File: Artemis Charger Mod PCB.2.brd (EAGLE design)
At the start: 99.1 x 96.5 mm, 156 parts, among them J1 MOLEX_CLICKMATE-2-VERTICAL, J2 MOLEX_CLICKMATE-4-VERTICAL, J3 MOLEX_CLICKMATE-2-VERTICAL, J4 MOLEX_CLICKMATE-2-VERTICAL, J5 MOLEX_CLICKMATE-2-VERTICAL, J6 MOLEX_CLICKMATE-4-VERTICAL, Q10 BSS138, Q11 BSS138, Q8 BSS138, Q9 BSS138, U10 TPS562219, U11 ISO7340, U12 ISO7340, U13 TPS562219, U14 MCP2515-TSSOP, U15 MCP2562, U16 CD4050BD, U17 CD4050BD, U18 CD4043B, U19 SN74LVC08ASOIC, U20 SN74LVC32ASOIC, U22 LTC1155, U23 CSD17506Q5A, U24 LTC1155, U25 CD4050BD, U26 CSD17506Q5A, U27 LTC1155, U28 CSD17506Q5A, U29 LTC1155, U3 MAX5812, U30 CSD17506Q5A, U31 LTC1155, U32 CSD17506Q5A, U33 LTC1155, U34 CSD17506Q5A, U49 TL7712A-SOIC, U8 MAX5812, U9 TPS562219

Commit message: DONE
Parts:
- moved R6 1.27 mm to (21.0, 58.4)
- moved C40 0.64 mm to (39.4, 50.2)
- moved U3 0.64 mm to (17.8, 58.4)
- moved U8 0.63 mm to (11.4, 58.4)
- moved Q8 0.63 mm to (41.3, 61.0)
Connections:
- removed net +5V/1_CURRENT_SENSE: O1.1
- net +3V3: now also O1.1
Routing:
- net GND1: track 386.0 -> 213.1 mm
- net GND: track 88.9 -> 61.7 mm
- net +3V3: track 117.8 -> 125.0 mm, vias 16 -> 17
- net +5V/1_CURRENT_SENSE: track 2.18 -> 0.00 mm, vias 1 -> 0
- net N$9: track 344.1 -> 342.3 mm
- net DRIVE_DISBALE_SIGNAL_3V3: track 101.3 -> 102.9 mm
- net N$7: track 47.1 -> 48.5 mm
- net N$1000: track 26.9 -> 27.8 mm
- net VBST_5V/1: track 6.99 -> 6.32 mm
- net VDD: track 152.9 -> 153.5 mm
- net N$58: track 97.7 -> 98.3 mm
- net N$4: track 6.07 -> 6.70 mm
- net RTDS_SOURCE: track 74.8 -> 75.4 mm
- net N$26: track 8.87 -> 9.40 mm
- net RSC_SIGNAL_3V3: track 78.6 -> 78.1 mm
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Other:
- board text added: "Formula Electric"
- board text added: "Missouri S&T"

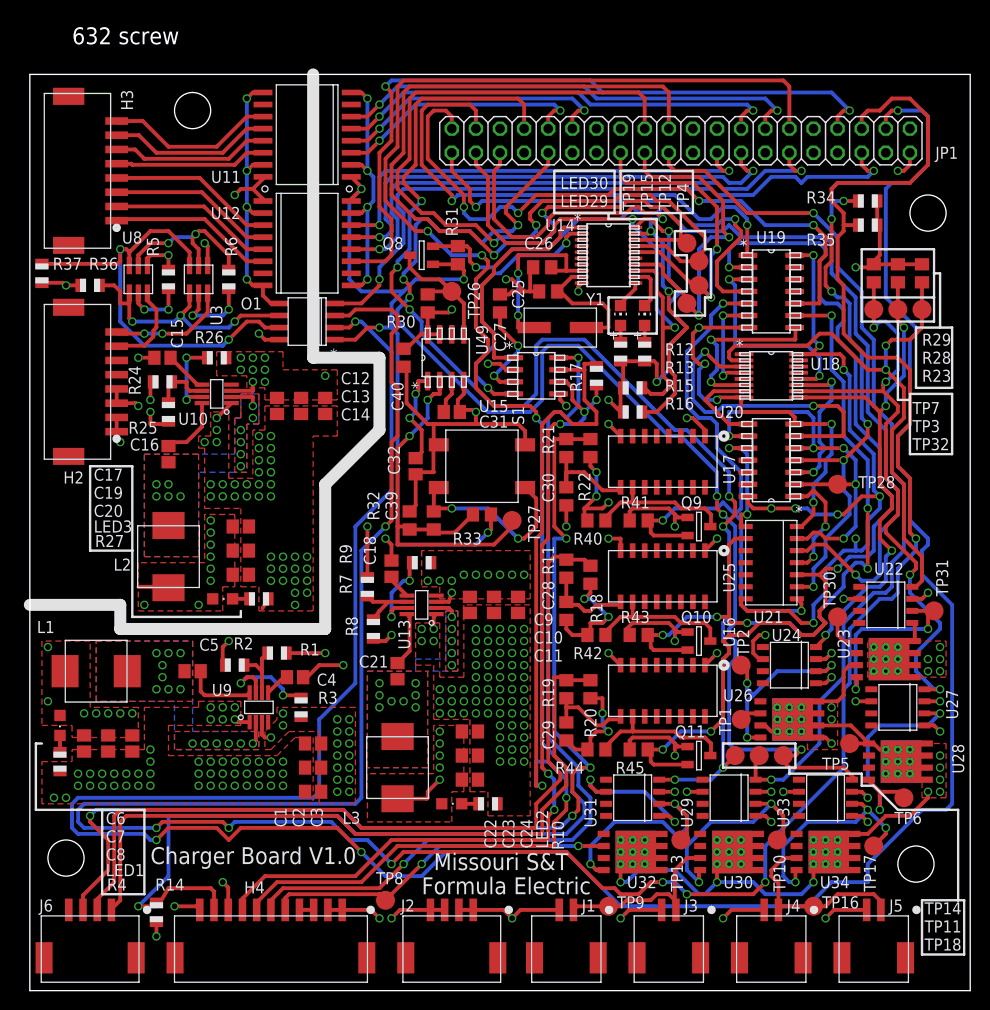
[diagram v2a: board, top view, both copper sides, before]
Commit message: Fixed list of errors: Too many vias around regulators
Make +5V plane in cover all area in isolated region

Make isolation barrier a simple rectangle

rotate +5v regulator (isolated area) 180deg so that the current path is more direct

More vias/planes at connectors

Give nets a descriptive name

Use vector font

U16/17/25 should combine into one part

bypass caps on ICs

U22/24/27/29/31/33 can be combined into 3 parts

RTDS_SOURCE is connected to FETs that it shouldn't be

U18 has a floating EN pin

use planes for current paths to the FETs, and make sure to connect to all of the pads (3 source, 4+pad drain)

Check pin current limits of connectors

Can use 10mil traces if needed for signals

Add mark to indicate pin 1 of RasPi connector

Watch mechanical clearances at the end of ICs, there are some that are really close

Q10/11 level shifters have pull downs. Does this work?

Label the connectors on the PCB so we know what they connect to.

Do we really need testpoints on every FET driver input/output?

Supply layer planes are a mess

Check RasPi power pins. There are multiple 5v and GND. Currently use 1 5V and no GND

RasPi Pin 6 is connected to the ground of one of the isolators, but not to the GND1 net

RasPi SPI interface is wired wrong

RasPi pin 39 is connected to the board as an I/O, but it is a GND pin
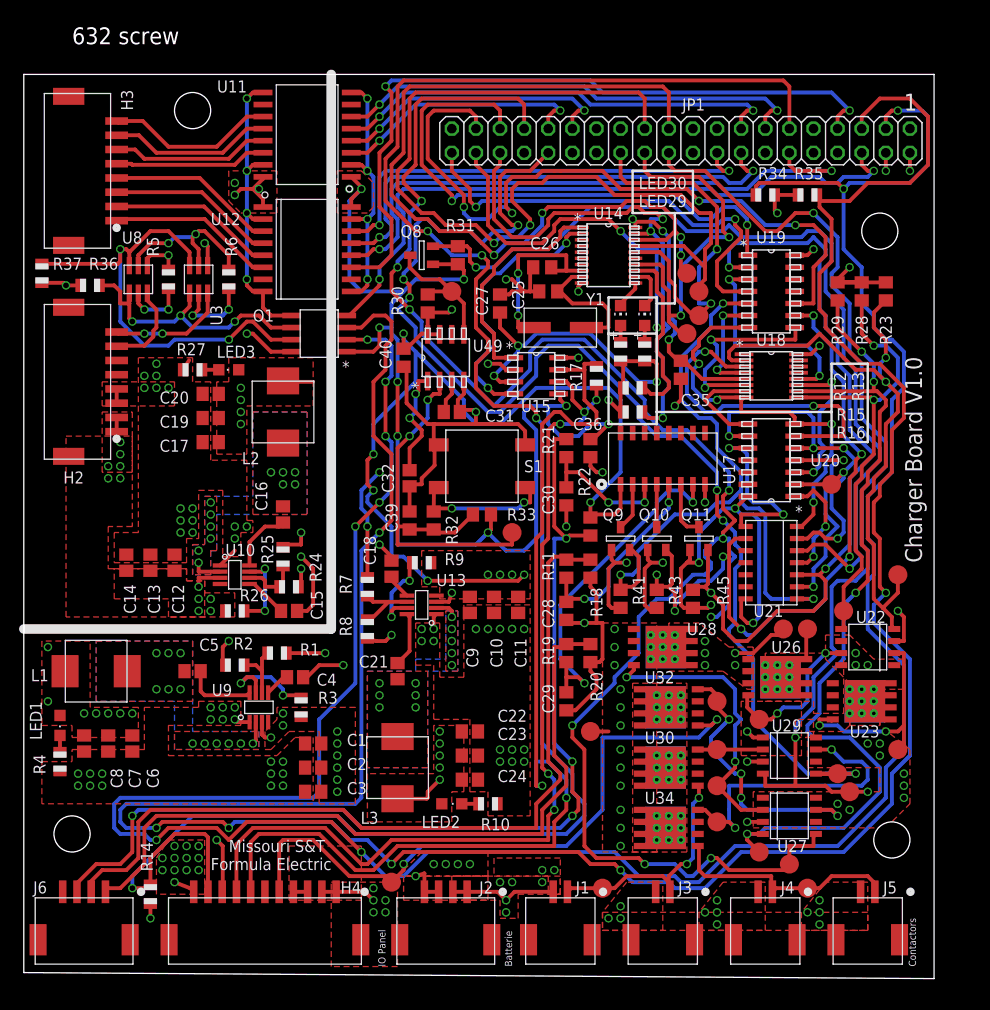
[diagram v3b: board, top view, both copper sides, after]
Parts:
- removed R40, R42, R44: 10k, rcl:R0805
- removed U16, U25: CD4050BD, FormE:SOIC-16
- removed U24, U31, U33: LTC1155, FormE:LT-SOL8
- added C35, C36: 1uF, rcl:C0805
- moved TP7 58.4 mm to (76.8, -1.91)
- moved TP3 32.3 mm to (85.7, 23.5)
- moved C15 29.8 mm to (27.3, 23.5), turned to 0 degrees
- moved TP32 28.1 mm to (91.4, 27.3)
- moved U28 27.5 mm to (66.7, 19.7)
- moved TP5 27.3 mm to (59.1, 10.8)
- moved R26 26.7 mm to (21.6, 23.5), turned to 0 degrees
- moved C14 26.7 mm to (10.2, 28.6), turned to 90 degrees
- moved R24 25.4 mm to (27.3, 26.0), turned to 0 degrees
- moved R27 25.1 mm to (17.1, 48.9), turned to 0 degrees
- moved LED3 24.1 mm to (21.0, 48.9), turned to 90 degrees
- moved C13 22.9 mm to (12.7, 28.6), turned to 90 degrees
- moved Q11 22.9 mm to (70.5, 31.1), turned to 0 degrees
- moved TP6 19.7 mm to (72.4, 5.08)
- moved C12 19.7 mm to (15.2, 28.6), turned to 90 degrees
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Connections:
- net MO renamed SO_SPI
- net N$10 renamed SCL1_I2C
- net N$1000 renamed SCL
- net N$11 renamed ADD
- net N$24 renamed ADJ_EMULATOR_IN_2
- net N$27 renamed ADJ_EMULATOR_IN_4
- net N$29 renamed ADJ_EMULATOR_IN_3
- net N$34 renamed LED_TO_PI_4
- net N$35 renamed LED_TO_PI_3
- net N$36 renamed LED_TO_PI_2
- net N$37 renamed LED_TO_PI_1
- net N$5 renamed ADJ_EMULATOR_IN_1
- net N$7 renamed SDA
- net N$70 renamed CS_SPI
- net RTDS_SOURCE2 renamed ACUMULATOR_CONTACTOR_SIGNAL
- net SCK renamed SCK_SPI
- removed net N$18: JP1.6, O1.4
- removed net N$48: H4.6, U15.8
- new net FET_CONNECT_1: TP30.TP, U23.1, U23.2, U23.3, U26.5, U26.6, U26.7, U26.8, U26.PAD, U26.PAD1, U26.VIA1, U26.VIA2, U26.VIA3, U26.VIA4, U26.VIA5, U26.VIA6, U26.VIA7, U26.VIA8, U26.VIA9
- new net FET_CONNECT_2: TP1.TP, U26.1, U26.2, U26.3, U28.5, U28.6, U28.7, U28.8, U28.PAD, U28.PAD1, U28.VIA1, U28.VIA2, U28.VIA3, U28.VIA4, U28.VIA5, U28.VIA6, U28.VIA7, U28.VIA8, U28.VIA9
- new net SDA1_I2C: JP1.3, O1.2, R34.2
- net +3V3: now also C35.1, C36.1, U14.20, U15.5, U18.16, U18.5, U19.14, U20.14, U21.14
- net +5V/1: now also JP1.4; no longer U14.20, U15.5
- net AMS_15V_FILTERED: now also U17.4; no longer R42.1, U25.10
- net AMS_BACK_TO_PI: now also JP1.37; no longer JP1.39
- net BSPD_FET_SIGNAL: now also U22.5; no longer U24.4
- net BSPD_FET_SIGNAL1: now also U27.5; no longer U31.4
- net BSPD_FET_SIGNAL3: now also U29.5; no longer U33.4
- net GND1: now also C35.2, C36.2, JP1.14, JP1.20, JP1.25, JP1.30, JP1.34, JP1.6, JP1.9, O1.4, U15.8; no longer R42.2, R44.2, U16.8, U24.3, U25.8, U31.3, U33.3
- net IMD_15V_FILTERED: now also U17.2; no longer R40.1, U17.10
- net INTERUPT_LINES_15V_FILTERED: now also U17.6; no longer R44.1, U16.10
- net INTERUPT_LINES_BACK_TO_PI: now also JP1.35; no longer JP1.37
- net N$43: now also U17.5; no longer U25.9
- net N$50: now also U17.7; no longer U16.9
- net N$53: now also U17.3; no longer U17.9
- net N$55: now also U22.7; no longer U24.2
- net N$59: now also U27.7; no longer U31.2
- net N$64: now also U29.7; no longer U33.2
- net N$9: no longer JP1.3, O1.2, R34.2
- net RTDS_SOURCE: no longer TP1.TP, TP30.TP, U23.1, U23.2, U23.3, U26.1, U26.2, U26.3, U26.5, U26.6, U26.7, U26.8, U26.PAD, U26.PAD1, U26.VIA1, U26.VIA2, U26.VIA3, U26.VIA4, U26.VIA5, U26.VIA6, U26.VIA7, U26.VIA8, U26.VIA9, U28.5, U28.6, U28.7, U28.8, U28.PAD, U28.PAD1, U28.VIA1, U28.VIA2, U28.VIA3, U28.VIA4, U28.VIA5, U28.VIA6, U28.VIA7, U28.VIA8, U28.VIA9
- net VDD: now also U22.8, U27.8, U29.8; no longer R40.2, U16.1, U18.16, U19.14, U20.14, U21.14, U24.1, U24.6, U25.1, U31.1, U31.6, U33.1, U33.6
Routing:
- net N$9: track 342.3 -> 23.0 mm, vias 10 -> 2
- net SDA1_I2C: track 0.00 -> 276.5 mm, vias 0 -> 9
- net +3V3: track 125.0 -> 227.2 mm, vias 17 -> 42
- net N$48: track 93.9 -> 0.00 mm, vias 2 -> 0
- net RTDS_SOURCE: track 75.4 -> 1.91 mm, vias 11 -> 12
- net N$18: track 71.4 -> 0.00 mm, vias 2 -> 0
- net GND1: track 213.1 -> 267.6 mm, vias 150 -> 80
- net BSPD_FET_SIGNAL1: track 131.8 -> 179.7 mm, vias 7 -> 9
- net VDD: track 153.5 -> 112.4 mm, vias 60 -> 37
- net ACUMULATOR_CONTACTOR_SIGNAL: track 38.0 -> 67.4 mm
- net RTDS_SIGNAL: track 64.4 -> 91.2 mm
- net N$50: track 9.63 -> 36.4 mm, vias 0 -> 2
- net DRIVE_DISBALE_SIGNAL_3V3: track 102.9 -> 83.4 mm, vias 4 -> 3
- net VCC: track 21.8 -> 5.96 mm, vias 10 -> 11
- net N$57: track 22.6 -> 6.86 mm, vias 2 -> 0
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- added copper zone on layer 1, net FET_CONNECT_1
- added copper zone on layer 1, net FET_CONNECT_2
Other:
- board size 99.1 x 96.5 mm -> 95.9 x 95.2 mm
- board text added: "1"
- board text added: "Batterie"
- board text added: "Contactors"
- board text added: "IO Panel"

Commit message: Started cleaning up layout
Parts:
- moved L2 3.81 mm to (26.7, 40.6)
- moved LED3 3.81 mm to (21.0, 45.1)
- moved R27 3.81 mm to (17.1, 45.1)
- moved C17 3.81 mm to (19.1, 37.5)
- moved C19 3.81 mm to (19.1, 40.0)
- moved C20 3.81 mm to (19.1, 42.5)
- moved C16 3.18 mm to (24.1, 31.8)
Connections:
- new net N$3: H4.3
- net GND1: now also JP1.39
- net N$25: now also H2.7; no longer H2.8
- net N$26: now also H2.8; no longer H2.7
- net N$42: no longer H4.3
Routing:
- net GND: track 67.7 -> 36.6 mm
- net GND1: track 267.6 -> 260.1 mm, vias 80 -> 79
- net +5V: track 36.1 -> 31.7 mm, vias 12 -> 13
- net VBST_5V: track 7.28 -> 3.03 mm
- net +5V/1: track 71.8 -> 68.0 mm, vias 18 -> 16
- net +3V3: track 227.2 -> 224.0 mm
- net VCC: track 5.96 -> 3.25 mm, vias 11 -> 0
- net SDA: track 50.3 -> 48.2 mm
- net N$42: track 1.50 -> 0.00 mm
- net SCL: track 29.6 -> 28.6 mm
- net N$26: track 9.40 -> 8.41 mm
- net LED_TO_PI_2: track 18.5 -> 17.5 mm
- net SW_5V: track 3.20 -> 2.26 mm, vias 11 -> 10
- net N$25: track 12.6 -> 13.1 mm, vias 2 -> 0
- net SW_3V3: track 2.39 -> 2.65 mm, vias 12 -> 10
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- removed copper zone on layer 15, net VCC
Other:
- board size 95.9 x 95.2 mm -> 95.9 x 94.6 mm
- board text removed: "632 screw"

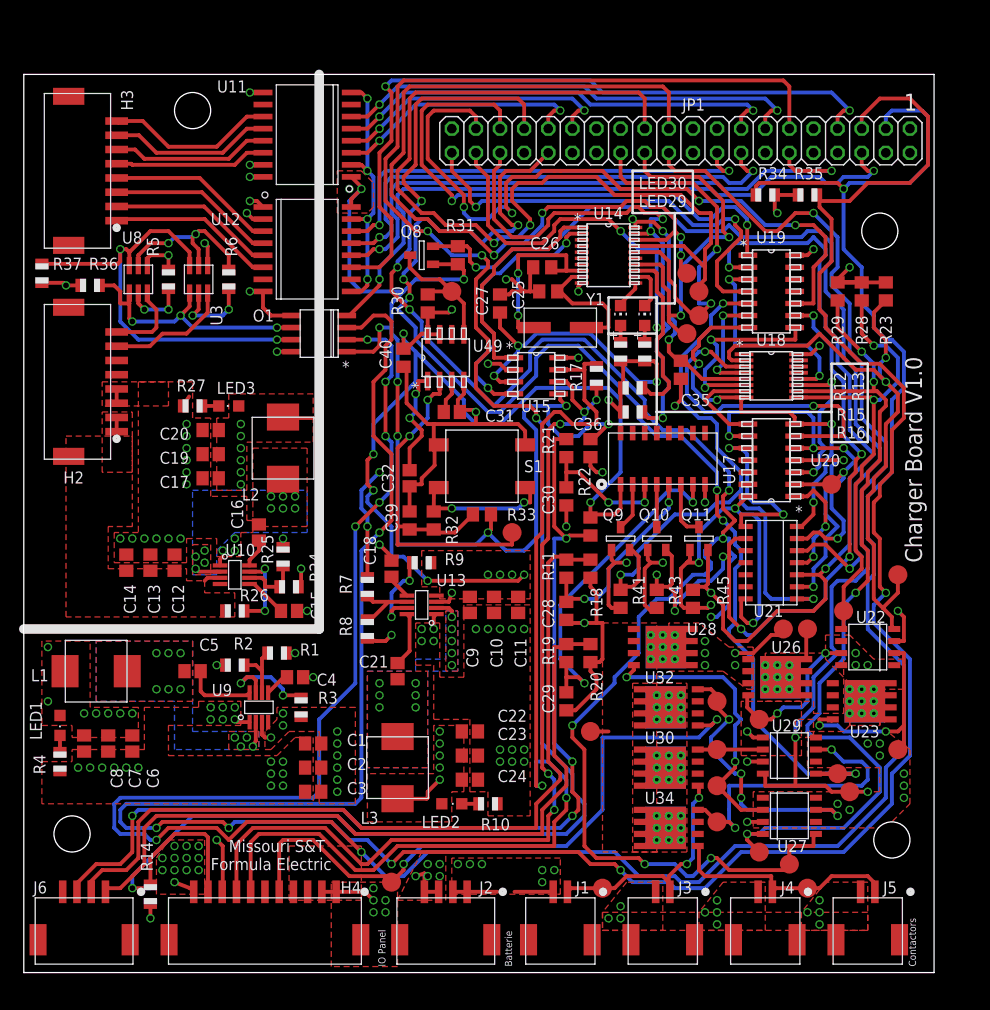
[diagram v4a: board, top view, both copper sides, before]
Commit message: Fixed second list of errors:  Decoupling capacitors
U11/12 EN pin is floating

Don't use solid planes at FET drivers

Lots of random vias

Planes from FETs to contactor connector

Connector labels

Cleanup supply layer planes

Isolation line needs to be thru center of isolators

unnecessary vias at raspi connector

SPI interface
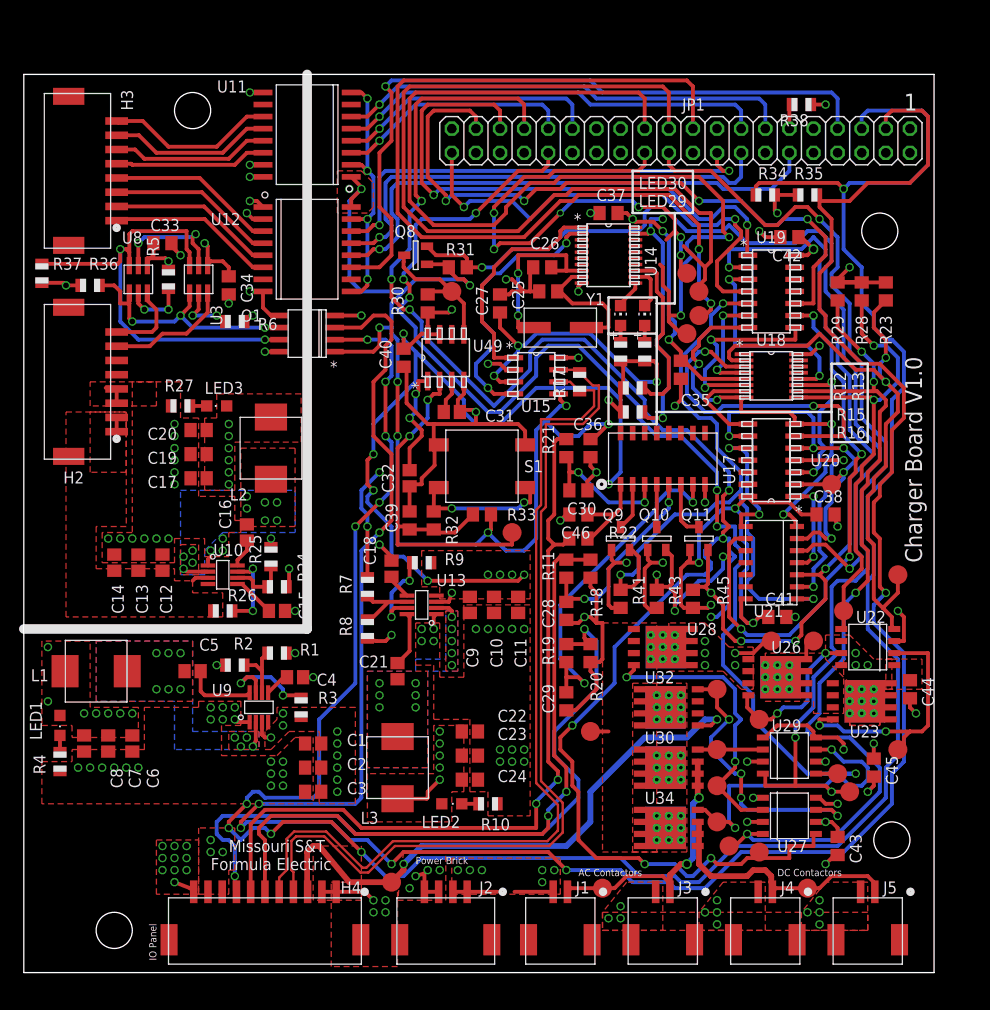
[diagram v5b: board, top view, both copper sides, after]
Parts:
- removed J6: MOLEX_CLICKMATE-4-VERTICAL, FormE:MOLEX-CLIKMATE-4-VERTICAL-HEADER
- removed R14: 10K, adafruit:R0805
- added C33, C34, C37, C38, C41, C42, C43, C44, C45, C46: 0.1uF, rcl:C0805
- added R38: 10K, adafruit:R0805
- moved TP19 6.35 mm to (69.2, 52.7)
- moved TP4 6.35 mm to (69.2, 59.1)
- moved R6 4.49 mm to (21.6, 54.0), turned to 0 degrees
- moved TP14 3.42 mm to (76.8, -1.91)
- moved TP7 3.24 mm to (73.7, -1.27)
- moved TP12 2.54 mm to (70.5, 57.1)
- moved TP15 2.54 mm to (70.5, 54.6)
- moved R17 1.89 mm to (57.9, 47.6)
- moved R22 1.80 mm to (57.8, 31.1), turned to 180 degrees
- moved TP1 1.80 mm to (78.1, 20.3)
- moved C30 1.42 mm to (57.8, 36.2), turned to 0 degrees
- moved TP30 1.42 mm to (82.5, 20.3)
- moved L2 1.27 mm to (25.4, 40.6)
- moved R25 1.27 mm to (25.4, 29.2)
- moved R31 1.27 mm to (45.1, 59.7), turned to 180 degrees
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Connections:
- net ADJ_EMULATOR_IN_1 renamed TIMER_ADJ_1
- net ADJ_EMULATOR_IN_2 renamed TIMER_ADJ_2
- net ADJ_EMULATOR_IN_3 renamed TIMER_ADJ_3
- net ADJ_EMULATOR_IN_4 renamed TIMER_ADJ_4
- removed net CAN_HIGH: H4.7, R17.1, U15.7
- removed net MI: JP1.26, TP12.TP, U14.16
- removed net N$38: JP1.18, U12.P$14
- removed net N$39: JP1.16, U12.P$13
- removed net N$40: JP1.12, U12.P$12
- removed net N$41: JP1.7, U12.P$11
- removed net N$42: H4.4
- removed net N$51: H4.8, R17.2, U15.6
- removed net N$52: H4.10, JP1.11, R14.1
- new net CAN_N: H4.5, R17.2, U15.6
- new net CAN_P: H4.4, R17.1, U15.7
- new net LED_TO_PI_1_C: H3.1, U12.P$6
- new net LED_TO_PI_2_C: H3.2, U12.P$5
- new net LED_TO_PI_3_C: H3.3, U12.P$4
- new net LED_TO_PI_4_C: H3.4, U12.P$3
- new net SI_SPI: JP1.19, TP15.TP, U14.16
- net +3V3: now also C37.1, C38.1, C41.1, C42.1
- net +5V: now also C33.1, C34.1
- net ACUMULATOR_CONTACTOR_SIGNAL: now also H4.3; no longer H4.5
- net AMS15V: now also H4.6; no longer J6.2
- net CS_SPI: now also JP1.24, TP4.TP; no longer JP1.21, TP19.TP
- net GND: now also C33.2, C34.2
- net GND1: now also C37.2, C38.2, C41.2, C42.2, C43.2, C44.2, C45.2, C46.2, H4.10, R38.1; no longer R14.2
- net IMD15V: now also H4.7; no longer J6.3
- net INTERUPT15V: now also H4.8; no longer J6.1
- net LED_TO_PI_1: now also JP1.18, U12.P$14; no longer H3.1, U12.P$6
- net LED_TO_PI_2: now also JP1.16, U12.P$13; no longer H3.2, U12.P$5
- net LED_TO_PI_3: now also JP1.12, U12.P$12; no longer H3.3, U12.P$4
- net LED_TO_PI_4: now also JP1.7, U12.P$11; no longer H3.4, U12.P$3
- net N$3: now also JP1.11, R38.2; no longer H4.3
- net N$49: no longer JP1.38
- net N$68: no longer JP1.36
- net SCK_SPI: now also JP1.23, TP19.TP; no longer JP1.24, TP4.TP
- net SCL1_I2C: now also JP1.3; no longer JP1.5
- net SDA1_I2C: now also JP1.5; no longer JP1.3
- net SO_SPI: now also JP1.21, TP12.TP; no longer JP1.23, TP15.TP
- net VDD: now also C43.1, C44.1, C45.1, C46.1
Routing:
- net N$52: track 210.9 -> 0.00 mm, vias 4 -> 0
- net CAN_HIGH: track 111.6 -> 0.00 mm, vias 2 -> 0
- net N$51: track 98.9 -> 0.00 mm, vias 5 -> 0
- net SI_SPI: track 0.00 -> 95.7 mm, vias 0 -> 2
- net CAN_P: track 0.00 -> 95.3 mm
- net CAN_N: track 0.00 -> 94.5 mm
- net N$41: track 77.1 -> 0.00 mm, vias 2 -> 0
- net N$40: track 64.7 -> 0.00 mm, vias 2 -> 0
- net SCK_SPI: track 39.7 -> 103.5 mm
- net GND1: track 260.1 -> 200.5 mm, vias 79 -> 87
- net LED_TO_PI_4: track 17.7 -> 75.7 mm, vias 0 -> 1
- net N$39: track 52.7 -> 0.00 mm, vias 2 -> 0
- net N$38: track 48.2 -> 0.00 mm, vias 2 -> 0
- net MI: track 40.3 -> 0.00 mm, vias 2 -> 0
- net LED_TO_PI_3: track 17.6 -> 56.1 mm, vias 0 -> 1
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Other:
- board text added: "AC Contactors"
- board text added: "DC Contactors"
- board text added: "Power Brick"
- board text removed: "Batterie"
- board text removed: "Contactors"
